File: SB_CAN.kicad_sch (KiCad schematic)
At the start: 88 parts, among them J1 XT30PB_IN, J2 USB_C_Receptacle_USB2.0_16P, J3 Excluder, J4 PT100, J5 Hotend, J6 FAN2, J7 LDC, J8 FS, J9 Conn_02x05_Odd_Even, Q1 BUK9M8R5-40EX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

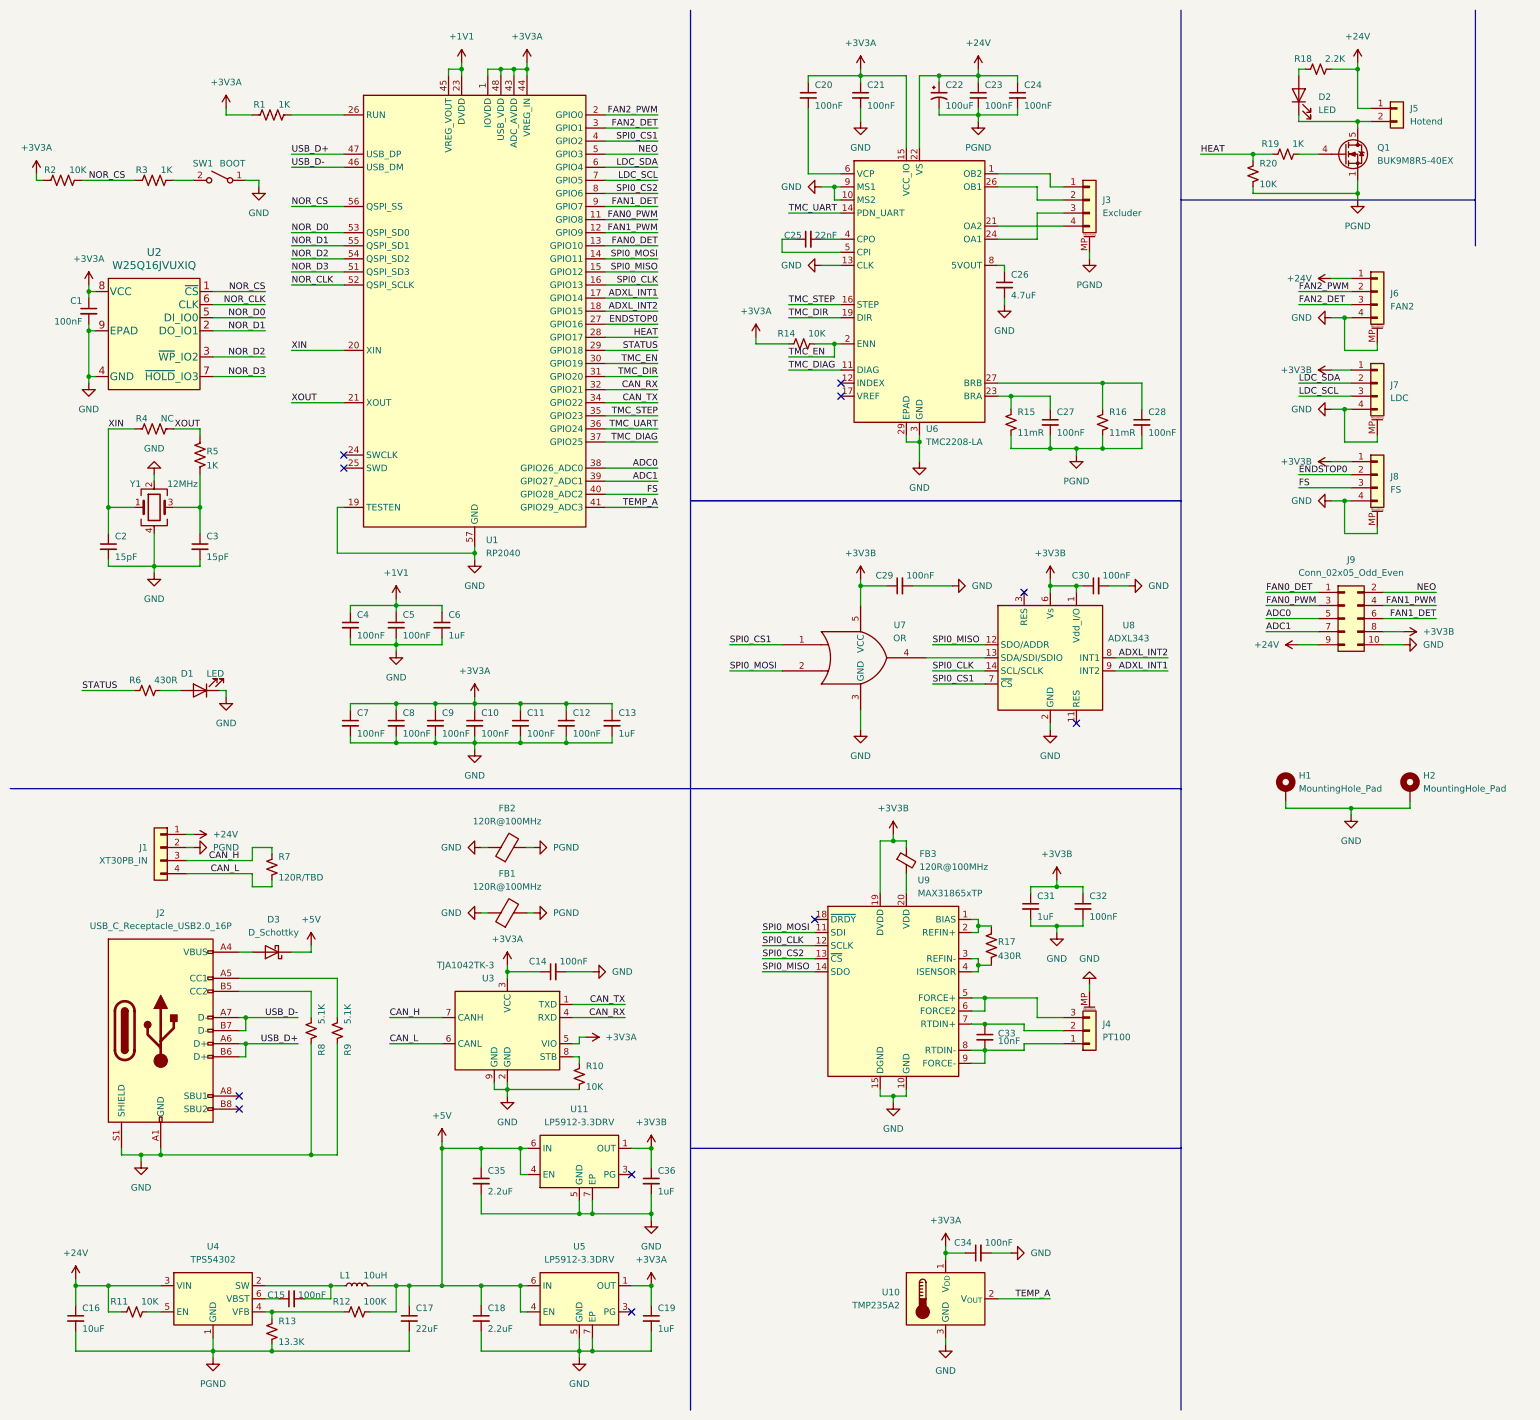
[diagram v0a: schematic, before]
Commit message: layout: optmise +3v3A power source: use new 3d models
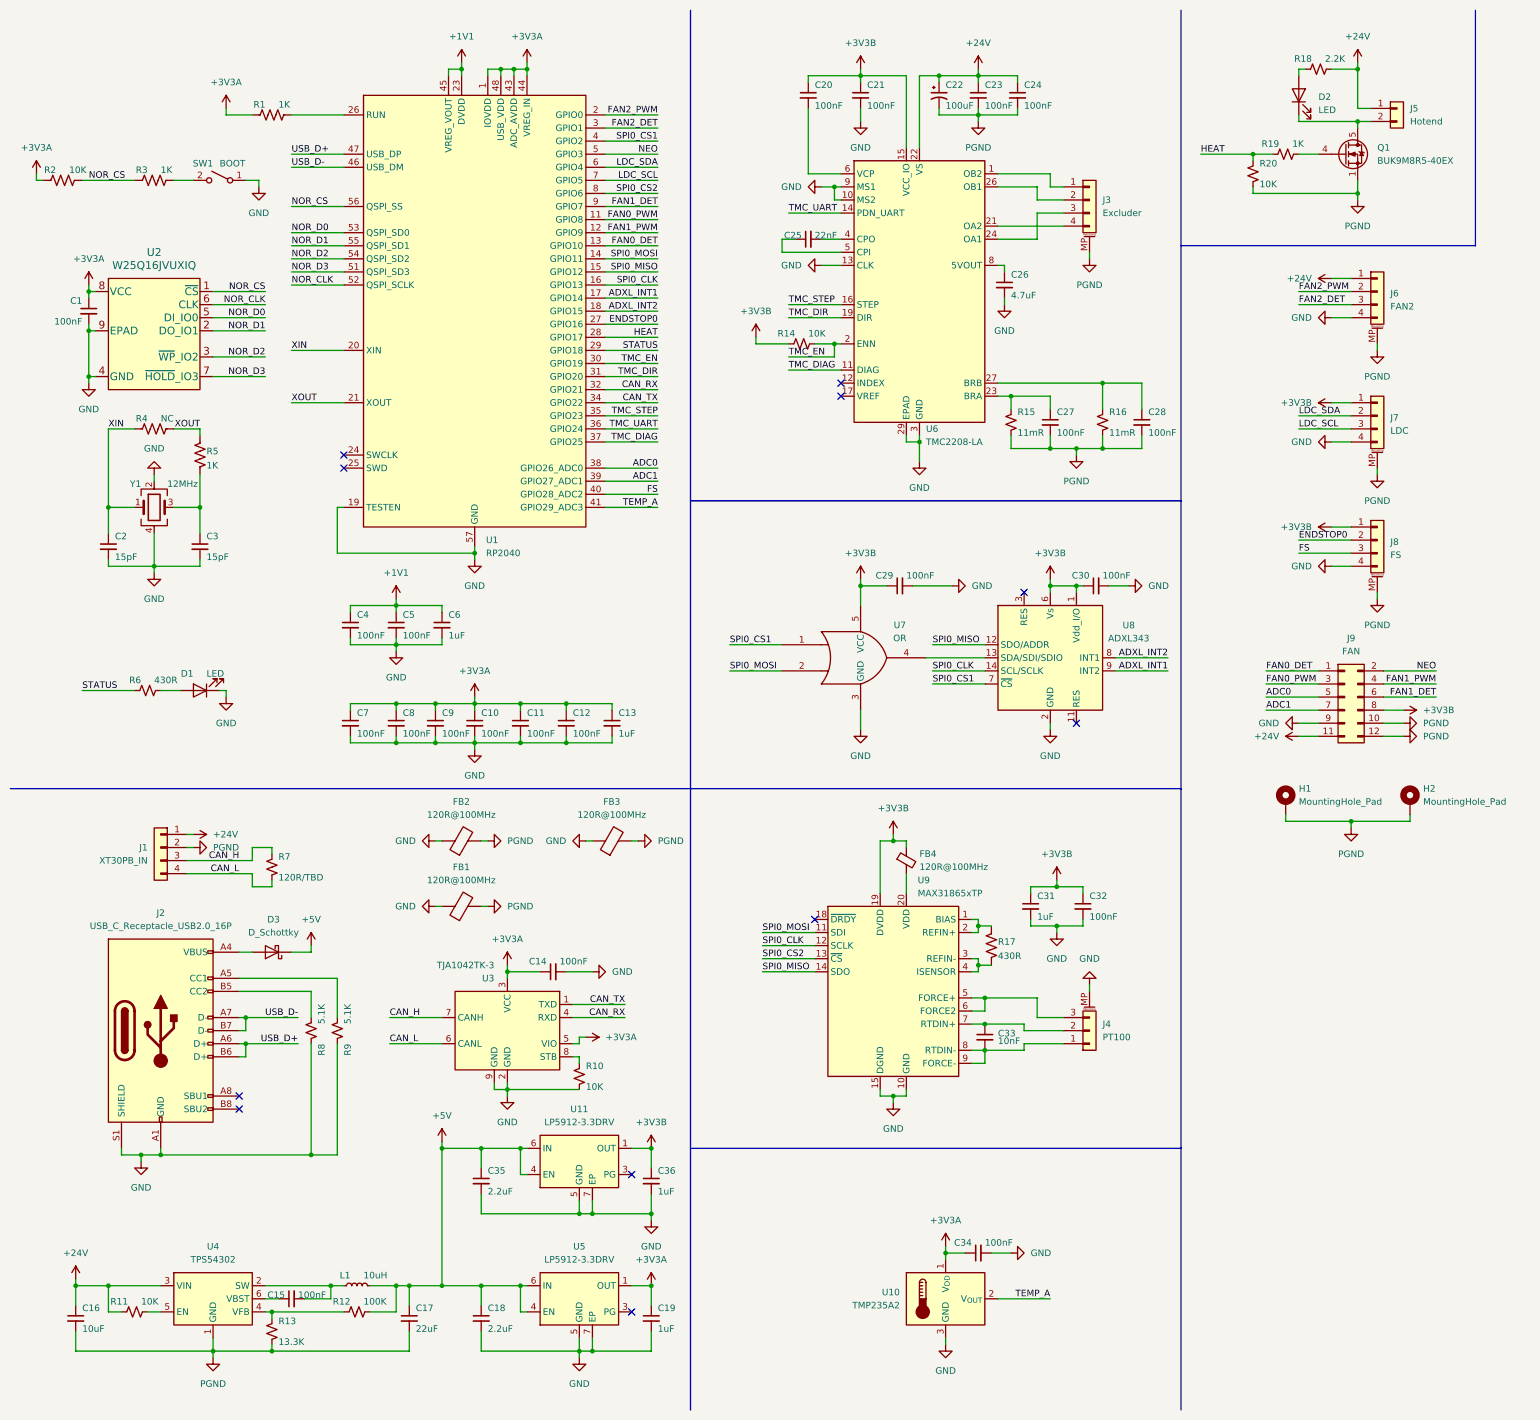
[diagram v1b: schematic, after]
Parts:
- added FB3: 120R@100MHz, Inductor_SMD:L_0603_1608Metric, symbol Device:FerriteBead
- J2: footprint Connector_USB:USB_C_Receptacle_XKB_U262-16XN-4BVC11 -> Connector_USB:USB_C_Receptacle_GCT_USB4105-xx-A_16P_TopMnt_Horizontal
- J5: footprint Connector_Molex:Molex_Micro-Fit_3.0_43045-0200_2x01_P3.00mm_Horizontal -> Library:Molex_Micro-Fit_3.0_43045-0200_2x01_P3.00mm_Horizontal
- J9: value Conn_02x05_Odd_Even -> FAN; footprint Connector_PinHeader_2.00mm:PinHeader_2x05_P2.00mm_Horizontal -> Connector_PinHeader_2.00mm:PinHeader_2x06_P2.00mm_Horizontal; symbol Connector_Generic:Conn_02x05_Odd_Even -> Connector_Generic:Conn_02x06_Odd_Even
- renumbered FB3 to FB4
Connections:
- net +24V: now also J9.11 (Pin_11); no longer J9.9 (Pin_9)
- net +3V3A: no longer C20.1, C21.1, R14.1, U6.15 (VCC_IO)
- net +3V3B: now also C20.1, C21.1, R14.1, U6.15 (VCC_IO)
- net GND: now also J9.9 (Pin_9), FB3.1; no longer H1.1, H2.1, J6.MP (MountPin), J7.MP (MountPin), J8.MP (MountPin), J9.10 (Pin_10)
- net PGND: now also H1.1, H2.1, J6.MP (MountPin), J7.MP (MountPin), J8.MP (MountPin), J9.10 (Pin_10), J9.12 (Pin_12), FB3.2
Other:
- moved on the sheet: FB1, FB2, H1, H2, J7, J8
